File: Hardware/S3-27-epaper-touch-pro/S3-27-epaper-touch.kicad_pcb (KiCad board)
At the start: 2 copper layers, 65.4 x 68 mm, 110 parts, among them J1 AFC24-S24FIC-00, J10 Conn_01x06_Pin, J2 Conn_01x06, J3 Conn_01x06, J4 TochConn, J5 Conn_01x03_Pin, J6 Conn_01x05_Pin, J7 Conn_01x04_Pin, J8 Conn_01x06, Q1 Si1308, Q2 Si2301, SW1 SW_Push, SW2 SW_Push, SW3 SW_Push, SW4 SW_Push, SW5 SW_Push, SW6 SW_Push, SW7 SW_Push, SW8 SW_Push, SW9 SW_Push, U1 ESP32-S3-WROOM-1-N8, U2 RT9013, U3 KoreanHropartsElecTYPE-C-31-M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, U5 BME680, U6 TPL5110, U7 RFM95W-868S2, U8 LSM6DSL

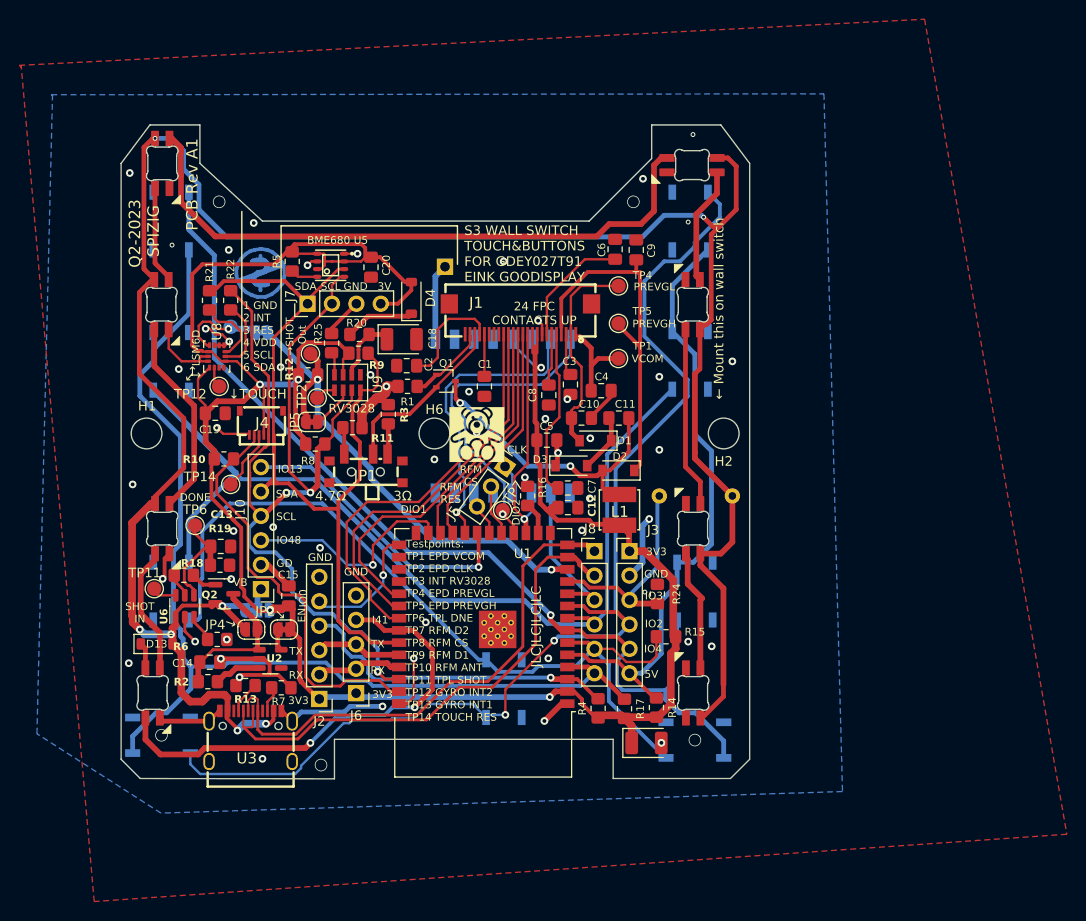
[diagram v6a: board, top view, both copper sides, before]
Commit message: Reworked Int Lines of I²C Connections
- Cleaned up Schematic
- added Micorphone Connector
- renamed RFM Miso Pins
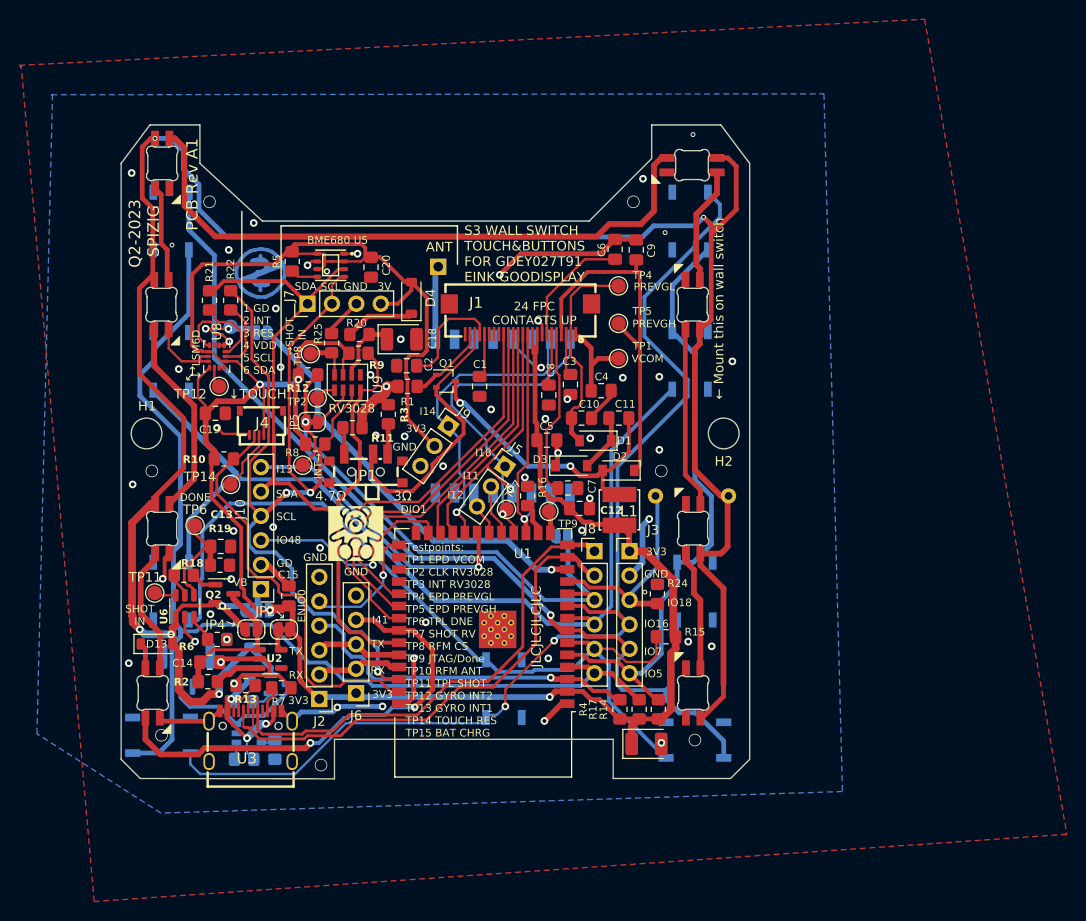
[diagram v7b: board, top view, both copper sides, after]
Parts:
- removed H6: MountingSwitch, MountingHole:MountingHole_3.2mm_M3
- added D14: MBR0530, Diode_SMD:D_SOD-123, B.Cu at (118.2, 114.0)
- added J11: Conn_01x02_Pin, Connector_JST:JST_GH_SM02B-GHS-TB_1x02-1MP_P1.25mm_Horizontal, B.Cu at (111.6, 114.6)
- added J9: Conn_01x03_Pin, Connector_PinHeader_2.54mm:PinHeader_1x03_P2.54mm_Vertical, F.Cu at (138.9, 89.3)
- added JP7: Jumper_2_Open, Jumper:SolderJumper-2_P1.3mm_Open_RoundedPad1.0x1.5mm, B.Cu at (150.7, 100.8)
- added Q3: Si2301, Package_TO_SOT_SMD:SOT-23, B.Cu at (121.3, 116.2)
- added R26: 800k, Resistor_SMD:R_0805_2012Metric_Pad1.20x1.40mm_HandSolder, B.Cu at (117.6, 124.0)
- added R27: 5k11, Resistor_SMD:R_0805_2012Metric_Pad1.20x1.40mm_HandSolder, B.Cu at (120.8, 123.0)
- added R28: 10K, Resistor_SMD:R_0805_2012Metric_Pad1.20x1.40mm_HandSolder, B.Cu at (117.5, 118.0)
- added TP8: SHOT IN, TestPoint:TestPoint_Pad_D1.5mm, F.Cu at (124.5, 81.8)
- added TP9: VCOM, TestPoint:TestPoint_Pad_D1.5mm, F.Cu at (149.3, 98.2)
- added U4: TP4065, tp4056:SOT-23-5_L3.0-W1.7-P0.95-LS2.8-BR, B.Cu at (118.1, 121.3)
- R20: value 100R -> N.C.
- R6: value 10K -> 220K
- U9: value ~ -> RV3032
- moved H3 16.3 mm to (129.2, 100.5)
- moved H4 15.7 mm to (127.9, 98.0)
- moved TP3 11.6 mm to (123.7, 93.4)
- moved R4 2.27 mm to (156.7, 118.8)
- moved R17 1.53 mm to (158.7, 118.8)
- moved C12 1.22 mm to (152.5, 97.9)
- moved TP10 0.70 mm to (137.8, 72.8)
- moved C1 0.50 mm to (142.1, 85.2)
- moved TP11 0.45 mm to (108.3, 106.7)
- moved TP7 0.41 mm to (144.9, 98.0)
- moved R23 0.40 mm to (168.0, 96.6)
- moved R14 0.27 mm to (160.7, 118.8)
- moved C16 0.10 mm to (159.5, 122.4)
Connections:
- J5 pad 1: /EPD_CLK -> /DIO2
- JP5 pad 1: /3231_INT -> /IO_17
- R12 pad 2: /3231_INT -> /IO_17
- TP3 pad 1: /3231_INT -> /IO_17
- U1 pad 15: unconnected-(U1-IO3-Pad15) -> Net-(U1-IO3)
- U3 pad A4: VBUS -> +5C
- U3 pad A9: VBUS -> +5C
- U3 pad B4: VBUS -> +5C
- U3 pad B9: VBUS -> +5C
- U7 pad 2: /IO_17 -> Net-(JP7-B)
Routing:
- net /IO_17: track 15.7 -> 60.4 mm, vias 0 -> 1
- net +3V3: track 234.7 -> 253.1 mm
- net GND: track 94.2 -> 111.4 mm, vias 53 -> 58
- net Net-(J11-Pin_1): track 0.00 -> 15.7 mm
- net +5C: track 0.00 -> 15.4 mm, vias 0 -> 3
- net Net-(JP1-C): track 18.4 -> 28.5 mm
- net /3231_INT: track 53.1 -> 45.6 mm, vias 2 -> 1
- net /TOUCH_SDA: track 93.6 -> 88.8 mm
- net Net-(JP7-B): track 0.00 -> 4.71 mm
- net /COL1: track 113.1 -> 117.8 mm
- net /IO_16: track 120.6 -> 117.9 mm
- net Net-(U1-IO3): track 0.00 -> 2.32 mm
- net Net-(Q3-G): track 0.00 -> 2.31 mm
- net Net-(U9-EVI): track 2.42 -> 4.67 mm
- net /ENABLE: track 33.5 -> 35.6 mm
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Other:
- board text added: "1 GD 2 INT 3 RES 4 VDD 5 SCL 6 SDA"
- board text added: "ANT"
- board text added: "Buttons: ■ Col/Row ■ C1/R1 4/7 ■ C2/R2 5/15 ■ C3/R3 6/16"
- board text added: "Documentation: github.com/uspizig/ WifiWallSwitch"
- board text added: "I11"
- board text added: "I12"
- board text added: "I13"
- board text added: "I14"
- board text added: "INT→"
- board text added: "IO16"
- board text added: "IO18"
- board text added: "IO5"
- board text added: "IO7"
- board text added: "TP15"
- board text added: "Testpoints: TP1 EPD VCOM TP2 CLK RV3028 TP3 INT RV3028 TP4 EPD PREVGL TP5 EPD PREVGH TP6 TPL DNE TP7 SHOT RV TP8 RFM CS TP9 JTAG/Done TP10 RFM ANT TP11 TPL SHOT TP12 GYRO INT2 TP13 GYRO INT1 TP14 TOUCH RES TP15 BAT CHRG"
- board text added: "→SHOT IN"
- board text added: "■ LORA MISO IO17 ■ LORA CS GPIO11 ■ LORA D1 GPIO14 ■ LORA D2 GPIO10"
- board text removed: "1 GND 2 INT 3 RES 4 VDD 5 SCL 6 SDA"
- board text removed: "5V"
- board text removed: "Buttons: ■ Column/Row ■ C1/R1 4/7 ■ C2/R2 5/15 ■ C3/R3 6/16"
- board text removed: "CLK"
- board text removed: "DIO2"
- board text removed: "Documentation: https://github.com/ uspizig/WifiWallSwitch"
- board text removed: "IO2"
- board text removed: "IO3"
- board text removed: "IO4"
- board text removed: "RFM CS"
- board text removed: "RFM RES"
- board text removed: "Testpoints: TP1 EPD VCOM TP2 EPD CLK TP3 INT RV3028 TP4 EPD PREVGL TP5 EPD PREVGH TP6 TPL DNE TP7 RFM D2 TP8 RFM CS TP9 RFM D1 TP10 RFM ANT TP11 TPL SHOT TP12 GYRO INT2 TP13 GYRO INT1 TP14 TOUCH RES"
- board text removed: "→SHOT Out"
- board text removed: "■ LORA MISO IO17 ■ LORA CS GPIO11 ■ LORA D1 GPIO12 ■ LORA D2 GPIO10"

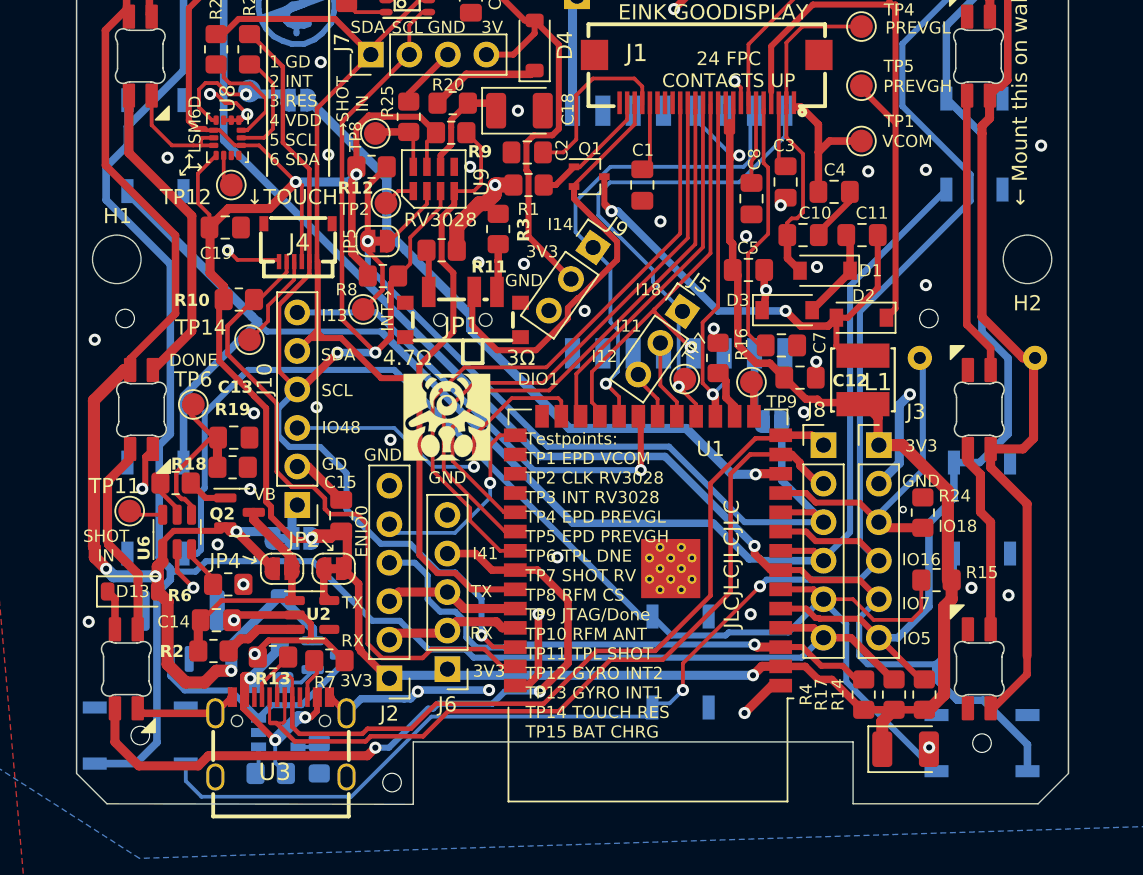
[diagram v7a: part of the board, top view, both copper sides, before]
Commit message: Finished for production
Added a dedicated Int Line for each I²C Sensor
Added several TP (GPIO3)
Rotated Battery Connector
Fixed Production files
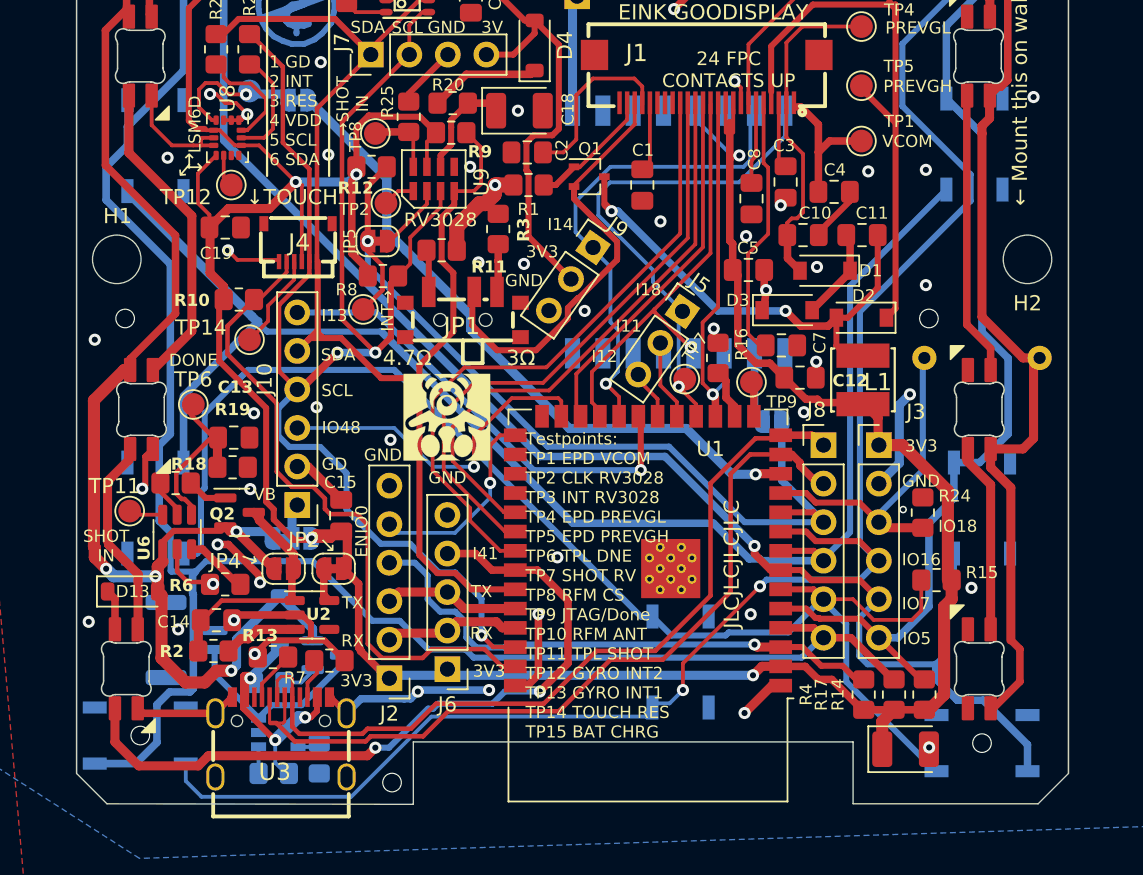
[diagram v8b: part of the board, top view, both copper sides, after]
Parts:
- moved J11 0.75 mm to (112.0, 115.2), turned to 90 degrees
- moved R23 0.30 mm to (168.3, 96.6)
- moved R26 0.20 mm to (117.8, 124.0)
- moved R6 0.20 mm to (114.6, 111.5), turned to 180 degrees
- moved JP4 0.10 mm to (118.5, 110.5)
- renumbered SW8 to SW3, SW3 to SW4, SW9 to SW5, SW7 to SW6, SW6 to SW7, SW4 to SW8, SW5 to SW9
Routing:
- net GND: track 111.4 -> 116.6 mm
- net Net-(J11-Pin_1): track 15.7 -> 13.3 mm
- net Net-(U6-DELAY/M_DRV): track 2.56 -> 4.18 mm
- net /COL1: track 117.8 -> 119.0 mm
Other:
- board text removed: "DIO1"
